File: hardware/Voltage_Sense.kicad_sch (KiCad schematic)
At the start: 56 parts, among them U6 TLV9002QDRQ1, U7 AMC3311QDWERQ1, U8 AMC3311QDWERQ1

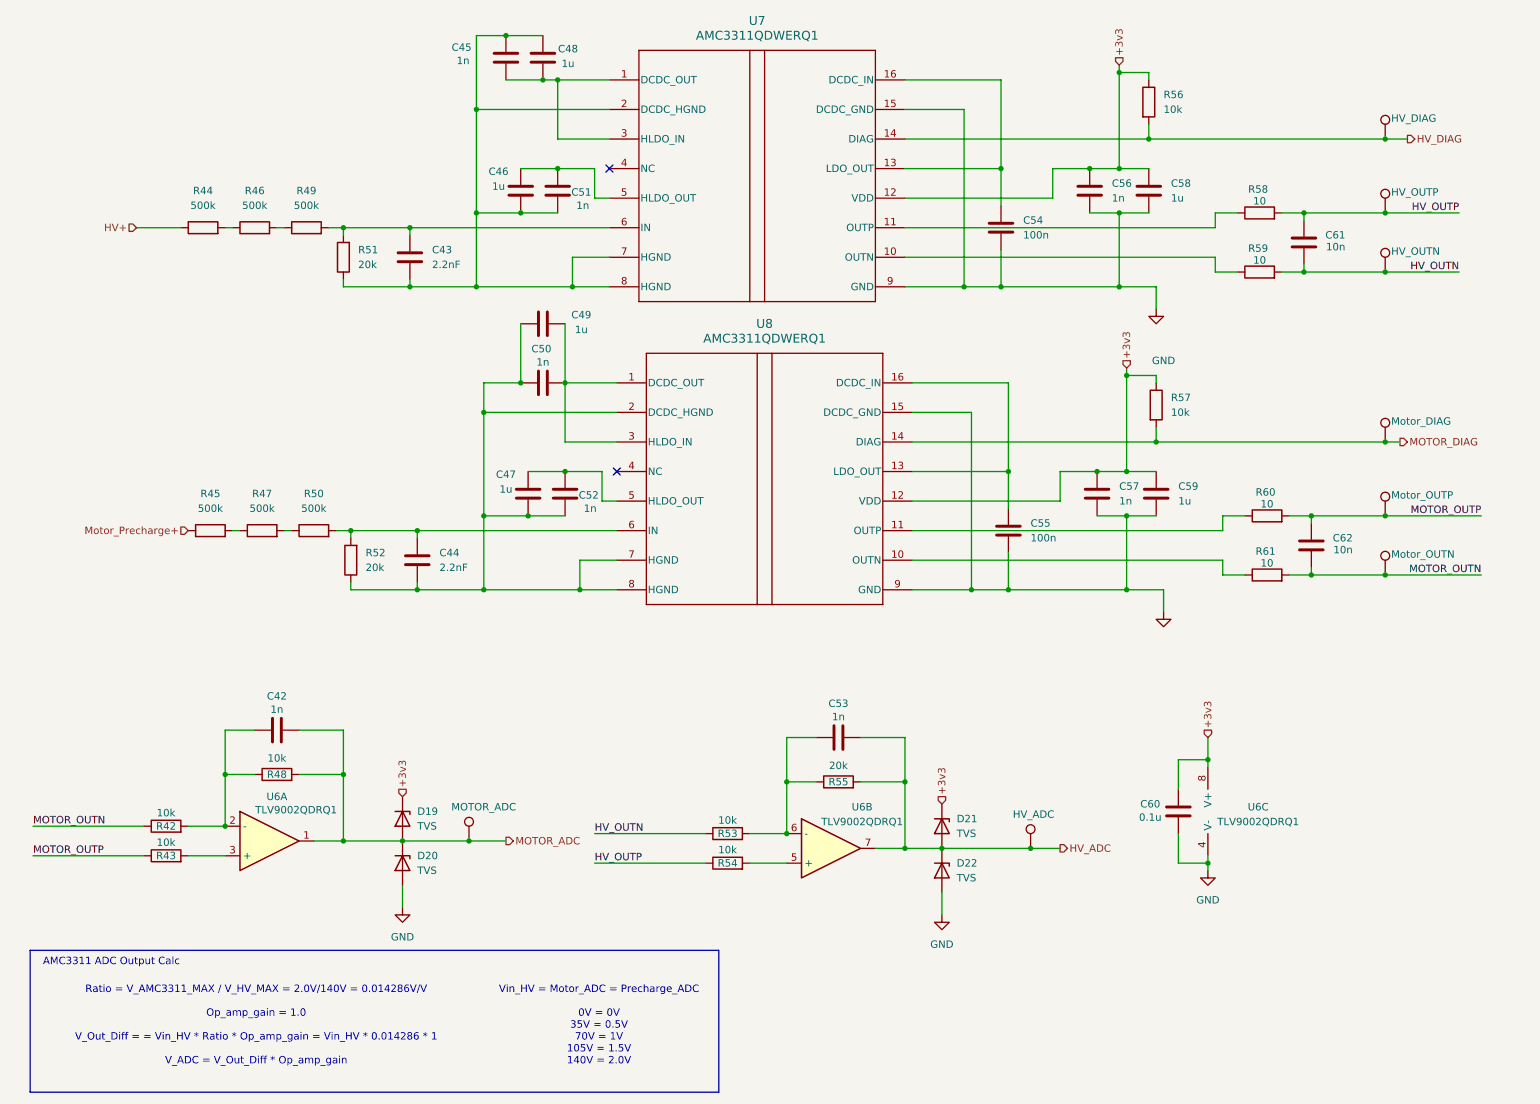
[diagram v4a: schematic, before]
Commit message: added USB power mux
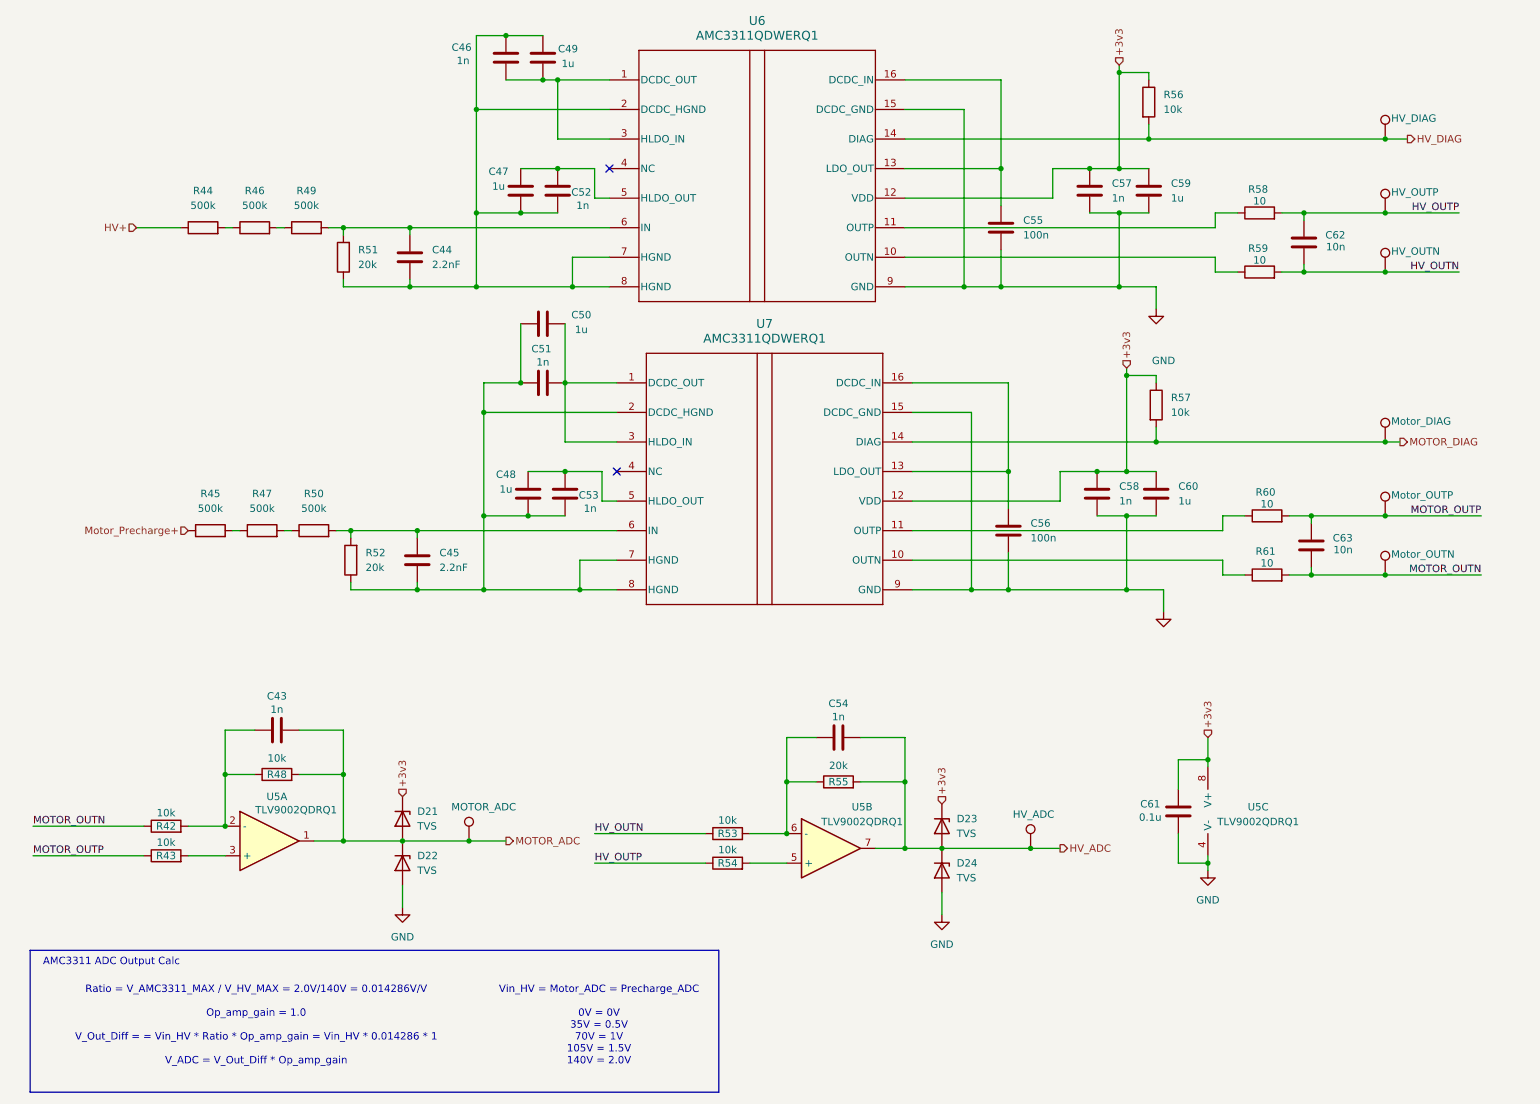
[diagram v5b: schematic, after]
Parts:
- renumbered C42 to C43, C43 to C44, C44 to C45, C45 to C46, C46 to C47, C47 to C48, C48 to C49, C49 to C50, C50 to C51, C51 to C52, C52 to C53, C53 to C54, C54 to C55, C55 to C56, C56 to C57, C57 to C58, C58 to C59, C59 to C60, C60 to C61, C61 to C62, C62 to C63, D19 to D21, D20 to D22, D21 to D23, D22 to D24, TP17 to TP21, TP18 to TP22, TP19 to TP23, TP20 to TP24, TP21 to TP25, TP22 to TP26, TP23 to TP27, TP24 to TP28, U6 to U5, U7 to U6, U8 to U7

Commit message: fixed ERC warnings
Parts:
- renumbered TP21 to TP22, TP22 to TP23, TP23 to TP24, TP24 to TP25, TP25 to TP26, TP26 to TP27, TP27 to TP28, TP28 to TP29
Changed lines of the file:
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@@
 		(in_pos_files yes)
 		(dnp no)
-		(property "Reference" "TP28"
+		(property "Reference" "TP29"
 			(at 248.92 103.3779 0)
 			(hide yes)
@@
 			(project "PS-HVCarrier"
 				(path "/2365a867-6254-4a7c-9718-f325e0bbac5c/83ab5b0b-4732-42c0-82fe-e74f4113c82a"
-					(reference "TP28")
+					(reference "TP29")
 					(unit 1)
 				)
@@
 		(in_pos_files yes)
 		(dnp no)
-		(property "Reference" "TP21"
+		(property "Reference" "TP22"
 			(at 91.44 149.0979 0)
 			(hide yes)
@@
 			(project "PS-HVCarrier"
 				(path "/2365a867-6254-4a7c-9718-f325e0bbac5c/83ab5b0b-4732-42c0-82fe-e74f4113c82a"
-					(reference "TP21")
+					(reference "TP22")
 					(unit 1)
 				)
@@
 		(in_pos_files yes)
 		(dnp no)
-		(property "Reference" "TP26"
+		(property "Reference" "TP27"
 			(at 248.92 80.5179 0)
 			(hide yes)
@@
 			(project "PS-HVCarrier"
 				(path "/2365a867-6254-4a7c-9718-f325e0bbac5c/83ab5b0b-4732-42c0-82fe-e74f4113c82a"
-					(reference "TP26")
+					(reference "TP27")
 					(unit 1)
 				)
@@
 		(in_pos_files yes)
 		(dnp no)
-		(property "Reference" "TP22"
+		(property "Reference" "TP23"
 			(at 187.96 150.3679 0)
 			(hide yes)
@@
 			(project "PS-HVCarrier"
 				(path "/2365a867-6254-4a7c-9718-f325e0bbac5c/83ab5b0b-4732-42c0-82fe-e74f4113c82a"
-					(reference "TP22")
+					(reference "TP23")
 					(unit 1)
 				)
@@
 		(dnp no)
 		(fields_autoplaced yes)
-		(property "Reference" "#PWR033"
+		(property "Reference" "#PWR032"
 			(at 215.9 165.1 0)
 			(hide yes)
@@
 			(project "PS-HVCarrier"
 				(path "/2365a867-6254-4a7c-9718-f325e0bbac5c/83ab5b0b-4732-42c0-82fe-e74f4113c82a"
-					(reference "#PWR033")
+					(reference "#PWR032")
 					(unit 1)
 				)
@@
 		(dnp no)
 		(fields_autoplaced yes)
-		(property "Reference" "#PWR029"
+		(property "Reference" "#PWR028"
 			(at 77.47 171.45 0)
 			(hide yes)
@@
 			(project "PS-HVCarrier"
 				(path "/2365a867-6254-4a7c-9718-f325e0bbac5c/83ab5b0b-4732-42c0-82fe-e74f4113c82a"
-					(reference "#PWR029")
+					(reference "#PWR028")
 					(unit 1)
 				)
@@
 		(in_pos_files yes)
 		(dnp no)
-		(property "Reference" "TP27"
+		(property "Reference" "TP28"
 			(at 248.92 93.2179 0)
 			(hide yes)
@@
 			(project "PS-HVCarrier"
 				(path "/2365a867-6254-4a7c-9718-f325e0bbac5c/83ab5b0b-4732-42c0-82fe-e74f4113c82a"
-					(reference "TP27")
+					(reference "TP28")
 					(unit 1)
 				)
@@
 		(in_pos_files yes)
 		(dnp no)
-		(property "Reference" "TP25"
+		(property "Reference" "TP26"
 			(at 248.92 51.3079 0)
 			(hide yes)
@@
 			(project "PS-HVCarrier"
 				(path "/2365a867-6254-4a7c-9718-f325e0bbac5c/83ab5b0b-4732-42c0-82fe-e74f4113c82a"
-					(reference "TP25")
+					(reference "TP26")
 					(unit 1)
 				)
@@
 		(dnp no)
 		(fields_autoplaced yes)
-		(property "Reference" "#PWR030"
+		(property "Reference" "#PWR029"
 			(at 170.18 172.72 0)
 			(hide yes)
@@
 			(project "PS-HVCarrier"
 				(path "/2365a867-6254-4a7c-9718-f325e0bbac5c/83ab5b0b-4732-42c0-82fe-e74f4113c82a"
-					(reference "#PWR030")
+					(reference "#PWR029")
 					(unit 1)
 				)
@@
 		(dnp no)
 		(fields_autoplaced yes)
-		(property "Reference" "#PWR032"
+		(property "Reference" "#PWR031"
 			(at 208.28 120.65 0)
 			(hide yes)
@@
 			(project "PS-HVCarrier"
 				(path "/2365a867-6254-4a7c-9718-f325e0bbac5c/83ab5b0b-4732-42c0-82fe-e74f4113c82a"
-					(reference "#PWR032")
+					(reference "#PWR031")
 					(unit 1)
 				)
@@
 		(in_pos_files yes)
 		(dnp no)
-		(property "Reference" "#PWR031"
+		(property "Reference" "#PWR030"
 			(at 207.01 68.58 0)
 			(hide yes)
@@
 			(project "PS-HVCarrier"
 				(path "/2365a867-6254-4a7c-9718-f325e0bbac5c/83ab5b0b-4732-42c0-82fe-e74f4113c82a"
-					(reference "#PWR031")
+					(reference "#PWR030")
 					(unit 1)
 				)
@@
 		(in_pos_files yes)
 		(dnp no)
-		(property "Reference" "TP24"
+		(property "Reference" "TP25"
 			(at 248.92 41.1479 0)
 			(hide yes)
@@
 			(project "PS-HVCarrier"
 				(path "/2365a867-6254-4a7c-9718-f325e0bbac5c/83ab5b0b-4732-42c0-82fe-e74f4113c82a"
-					(reference "TP24")
+					(reference "TP25")
 					(unit 1)
 				)
@@
 		(in_pos_files yes)
 		(dnp no)
-		(property "Reference" "TP23"
+		(property "Reference" "TP24"
 			(at 248.92 28.4479 0)
 			(hide yes)
@@
 			(project "PS-HVCarrier"
 				(path "/2365a867-6254-4a7c-9718-f325e0bbac5c/83ab5b0b-4732-42c0-82fe-e74f4113c82a"
-					(reference "TP23")
+					(reference "TP24")
 					(unit 1)
 				)

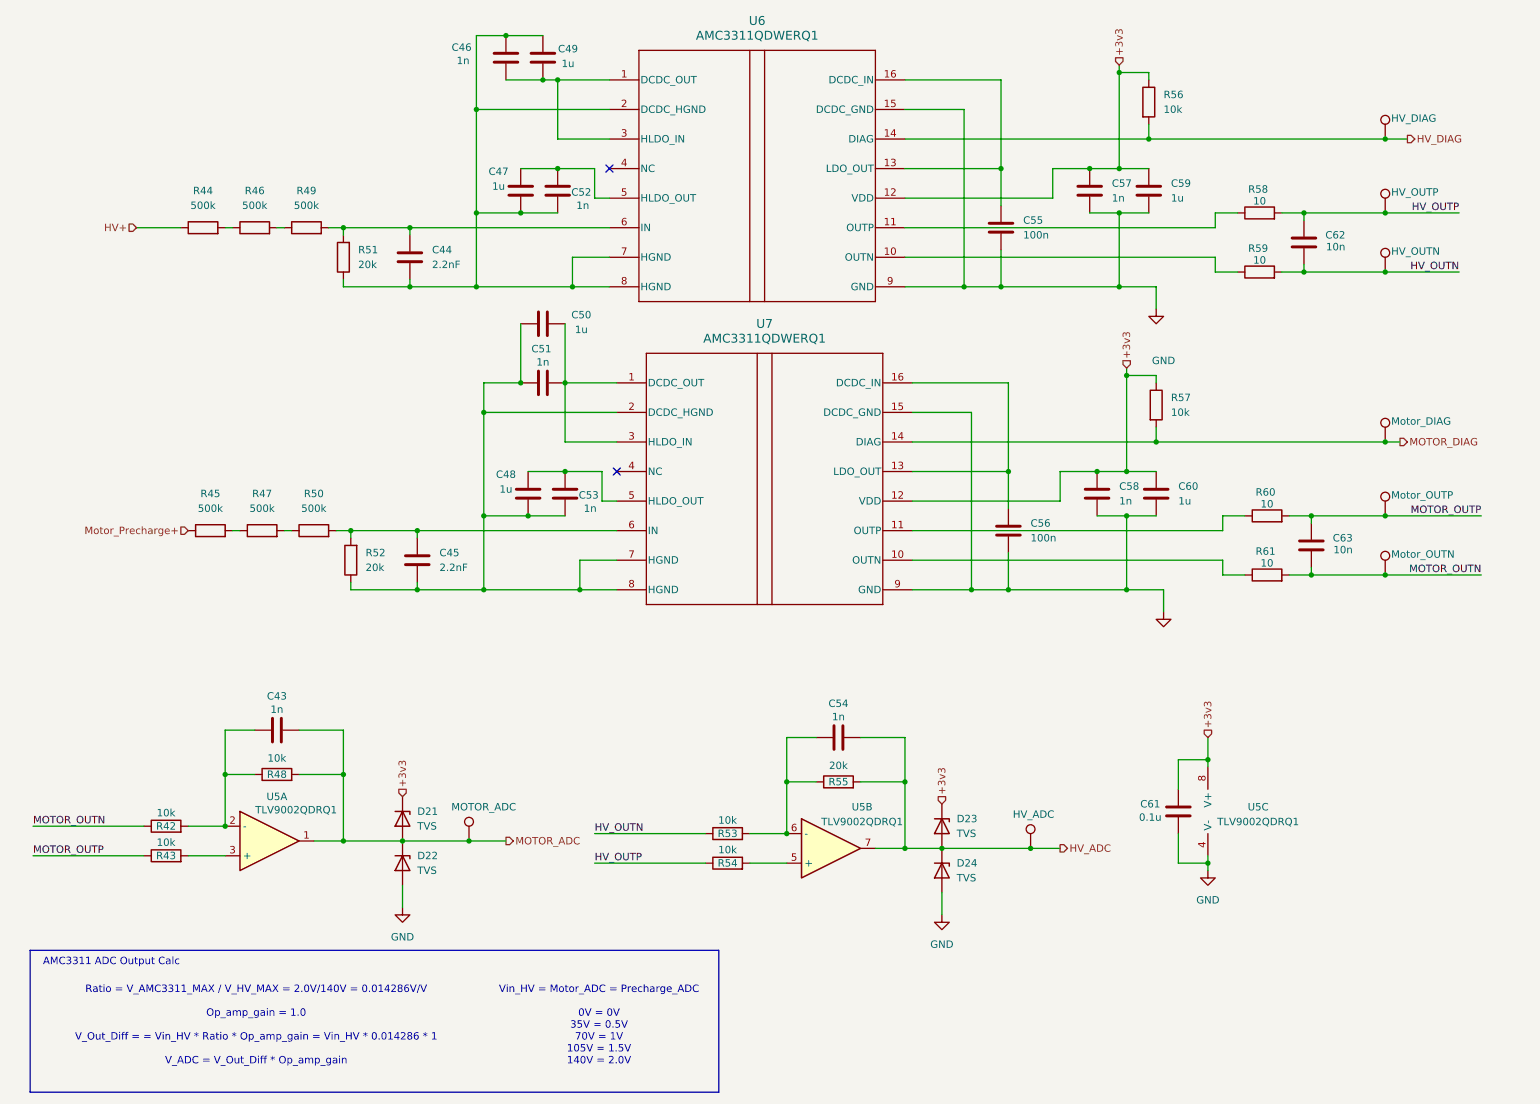
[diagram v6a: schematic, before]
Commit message: added pin layout ss, resolved erc errors, added p/n
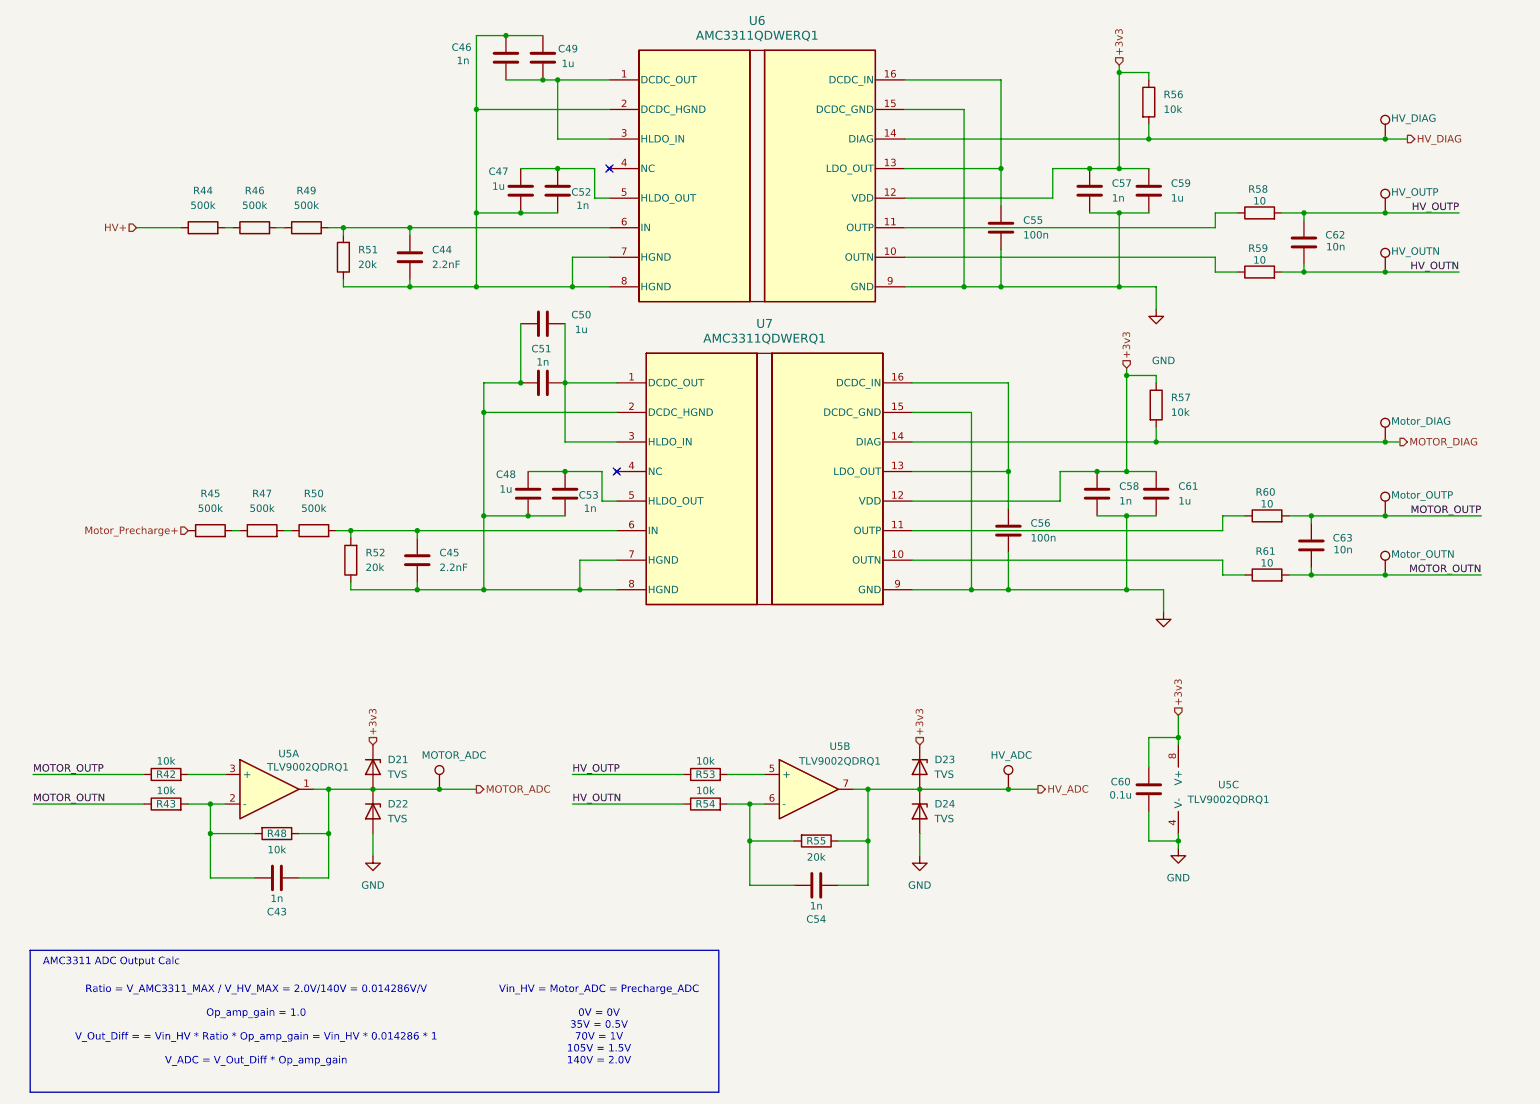
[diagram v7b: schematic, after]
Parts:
- U6, U7: footprint DWE0016A-IPC_A -> AMC3311QDWERQ1:DWE0016A-IPC_A
- renumbered C61 to C60, C60 to C61, R43 to R42, R42 to R43, R54 to R53, R53 to R54
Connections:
- net HV_ADC: now also C54.2, R55.1; no longer C54.1, R55.2
- net MOTOR_ADC: now also C43.2, R48.1; no longer C43.1, R48.2
- net at R43.2, U5.2 (-): now also C43.1, R48.2; no longer C43.2, R48.1
- net at R54.2, U5.6 (-): now also C54.1, R55.2; no longer C54.2, R55.1
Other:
- moved on the sheet: C43, C54, C60, D21, D22, D23, D24, R42, R43, R48, R53, R54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

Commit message: added 1% calcs
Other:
- note added: "+-1% Tolerance Nominal: 1.5M + 20k divider, ratio of 0.013158 140 * 0.013158 = 1.8421 Highest reading: 1,485,000 (min) + 20,200 (max), ratio of 0.013419 140* 0.013419 = 1.8787 (+1.99%) Lowest reading: 1,515,000 (max) + 19,800 (min), ratio of 0.012900 140 * 0.012900 = 1.8060 (-1.96%)"
- note added: "1% Resistor Divider Worst Case"
- note added: "Voltage Error @ 140V for 1% tolerance Divider error: +-2% and +-2.8V difference"
- moved on the sheet: C43, C54, C60, D21, D22, D23, D24, R42, R43, R48, R53, R54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
